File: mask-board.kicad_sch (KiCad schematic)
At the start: 58 parts, among them J1 SWIM Connector, J2 I2C Breakout, M1 Fan_3pin, M2 Fan_3pin, M3 Motor_DC, Q1 2N7000, Q2 2N7000, Q3 2N7000, Q4 2N7000, SW1 SW_Push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

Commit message: Update to board V2
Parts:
- D1: footprint footprints:T2133BGR -> footprints:LED_T2133BGR
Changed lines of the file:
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@@
 			)
 		)
-		(property "Footprint" "footprints:T2133BGR"
+		(property "Footprint" "footprints:LED_T2133BGR"
 			(at 252.73 140.97 0)
 			(effects

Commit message: Update to V3
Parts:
- removed D2, D3, D4: D_Schottky, Package_TO_SOT_SMD:SOT-23-3, symbol Device:D_Schottky
- removed Q1, Q2, Q3, Q4: 2N7000, Package_TO_SOT_THT:TO-92_Inline, symbol Transistor_FET:2N7000
- added D2, D3, D4: PMEG4010ER, Diode_SMD:Nexperia_CFP3_SOD-123W, symbol Diode:PMEG4010ER
- added Q1, Q2, Q3, Q4: DMN10H220L, Package_TO_SOT_SMD:SOT-23, symbol Transistor_FET:DMN10H220L
- M1, M2: footprint Connector_PinHeader_2.54mm:PinHeader_1x03_P2.54mm_Vertical -> footprints:JST-XH-3-pin
- M3: footprint Connector_PinHeader_2.54mm:PinHeader_1x02_P2.54mm_Vertical -> footprints:JST-XH-2-pin
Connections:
- net +3V3: now also D2.1 (K)
- net +5V: now also D3.1 (K), D4.1 (K)
- net GND: now also Q1.2 (S), Q2.2 (S), Q3.2 (S), Q4.2 (S)
- net at R14.2: now also Q4.1 (G)
- net at R12.2: now also Q3.1 (G)
- net at M3.2 (-): now also D2.2 (A), Q2.3 (D)
- net at M2.1 (-): now also D4.2 (A), Q4.3 (D)
- net at M1.1 (-): now also D3.2 (A), Q3.3 (D)
- net at R11.2: now also Q2.1 (G)
- net at R16.2: now also Q1.1 (G)
- net at BZ1.2 (-): now also Q1.3 (D)

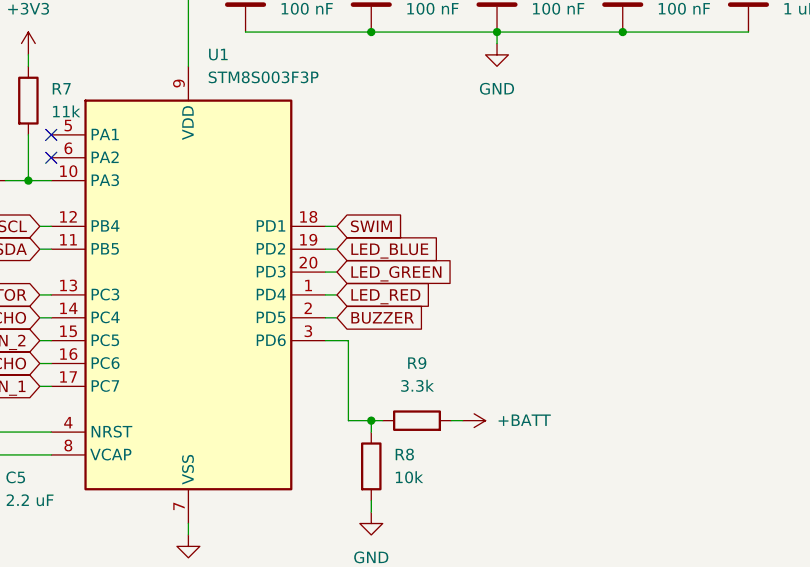
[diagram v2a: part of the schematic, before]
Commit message: Update to V4; Add quarter for scale in 3D model
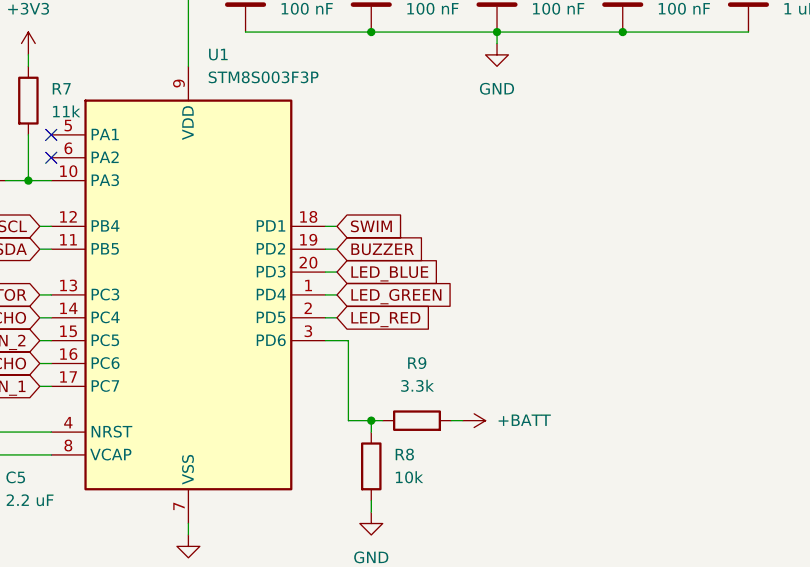
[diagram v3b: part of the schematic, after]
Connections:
- net BUZZER: now also U1.19 (PD2); no longer U1.2 (PD5)
- net LED_BLUE: now also U1.20 (PD3); no longer U1.19 (PD2)
- net LED_GREEN: now also U1.1 (PD4); no longer U1.20 (PD3)
- net LED_RED: now also U1.2 (PD5); no longer U1.1 (PD4)
